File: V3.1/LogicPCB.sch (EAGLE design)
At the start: 65 parts, among them CON1 CUBE_ORANGE_, CON10 PINHEAD_1X02-2.54, CON11 CON-4P-JST-XA, CON12 PINHEAD_1X06-2.54, CON13 CON-6P-JST-XA, CON14 PINHEAD_1X04-2.54, CON15 CON-4P-JST-XA, CON17 CON-4P-JST-XA, CON18 CON-6P-JST-XA, CON19 USB-TYPE-C-VERT-PROD, CON2 CON-4P-JST-XA, CON20 PINHEAD_1X06-2.54, CON21 CON-4P-JST-XA, CON22 CON-4P-JST-XA, CON23 CON-4P-JST-XA, CON24 CON-4P-JST-XA, CON25 CON-4P-JST-XA, CON26 CON-4P-JST-XA, CON27 CON-4P-JST-XA, CON28 CON-4P-JST-XA, CON29 CON-4P-JST-XA, CON3 RJ45-NO_SHIELD-5556416-1, CON30 CON-4P-JST-XA, CON32 CON-4P-JST-XA, CON35 CON-12P-JST-XA, CON4 CON-2P-JST-XA, CON5 CON-6P-JST-XA, CON6 CON-4P-JST-XA, CON7 PINHEAD_1X06-2.54, CON9 PINHEAD_1X12-2.54, IC5 AOZ1280, M1 05G_ETHERNET_SWITCH, Q1 IRLML0030, T1 H1102NL, T2 H1102NL, T3 H1102NL, T4 H1102NL

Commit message: uarts
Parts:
- added R4, R5: (no value), rc:R-1%-0603
- added R6, R7: 000, rc:R-1%-0603
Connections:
- new net N$10: CON18.4, R5.1
- new net N$9: CON18.3, R4.1
- net GND: no longer CON35.10
- net HLK_RX0: now also CON35.6
- net HLK_RX1: now also R6.1
- net HLK_TX0: now also CON35.5
- net HLK_TX1: now also R7.1
- net SERIAL1_RX: now also R5.2, R7.2; no longer CON18.4
- net SERIAL1_TX: now also R4.2, R6.2; no longer CON18.3
- net SERIAL3_RX: now also CON35.8; no longer CON35.6
- net SERIAL3_TX: now also CON35.7; no longer CON35.5
- net VDD_24V: now also CON35.10; no longer CON35.7, CON35.8

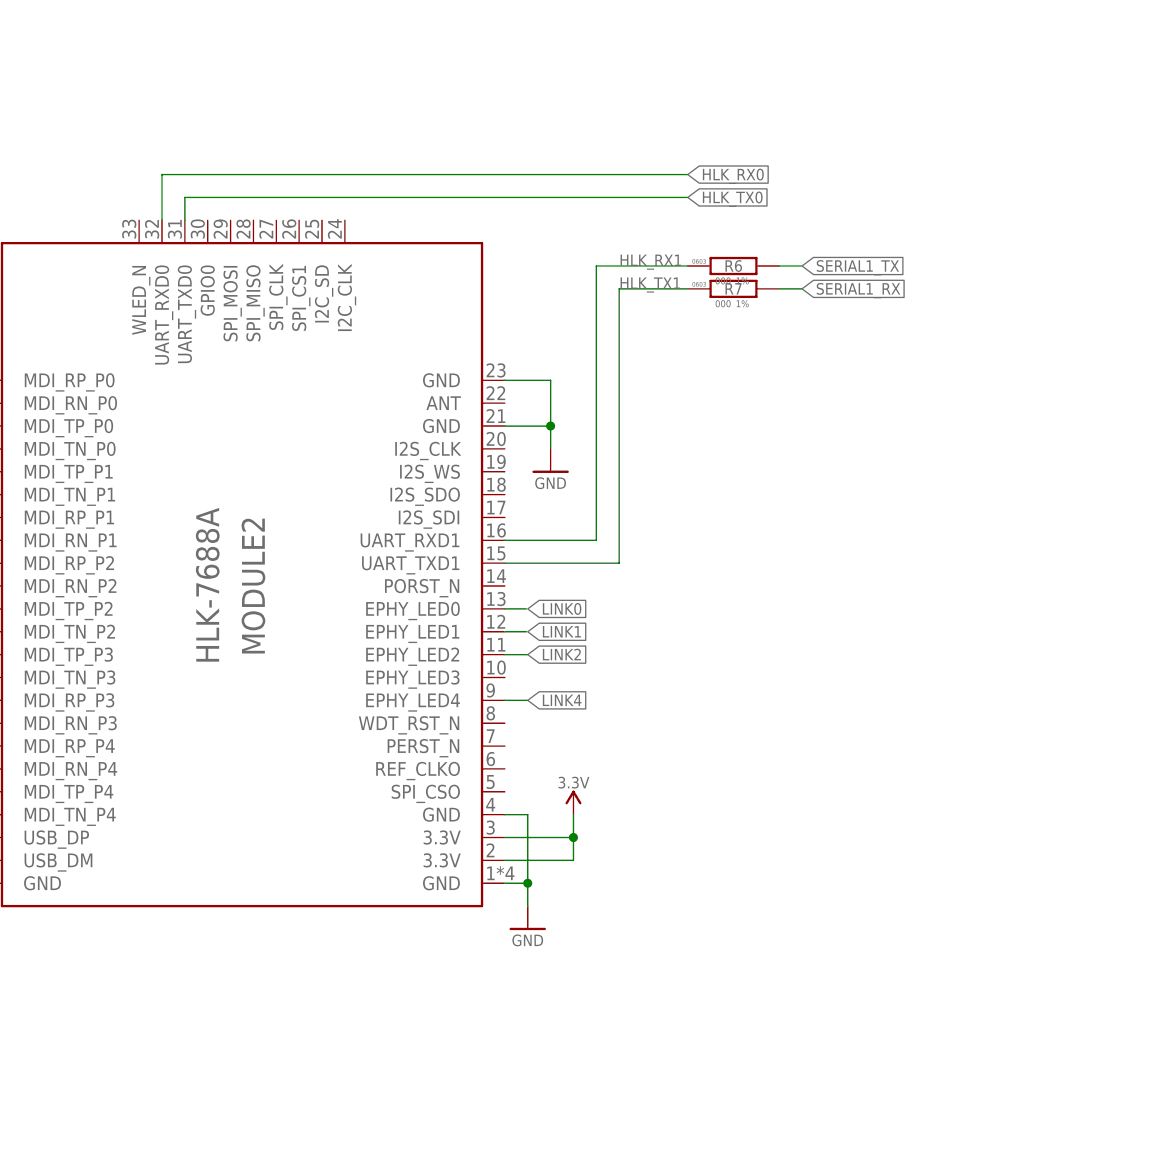
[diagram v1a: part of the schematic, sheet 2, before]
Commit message: link leds added
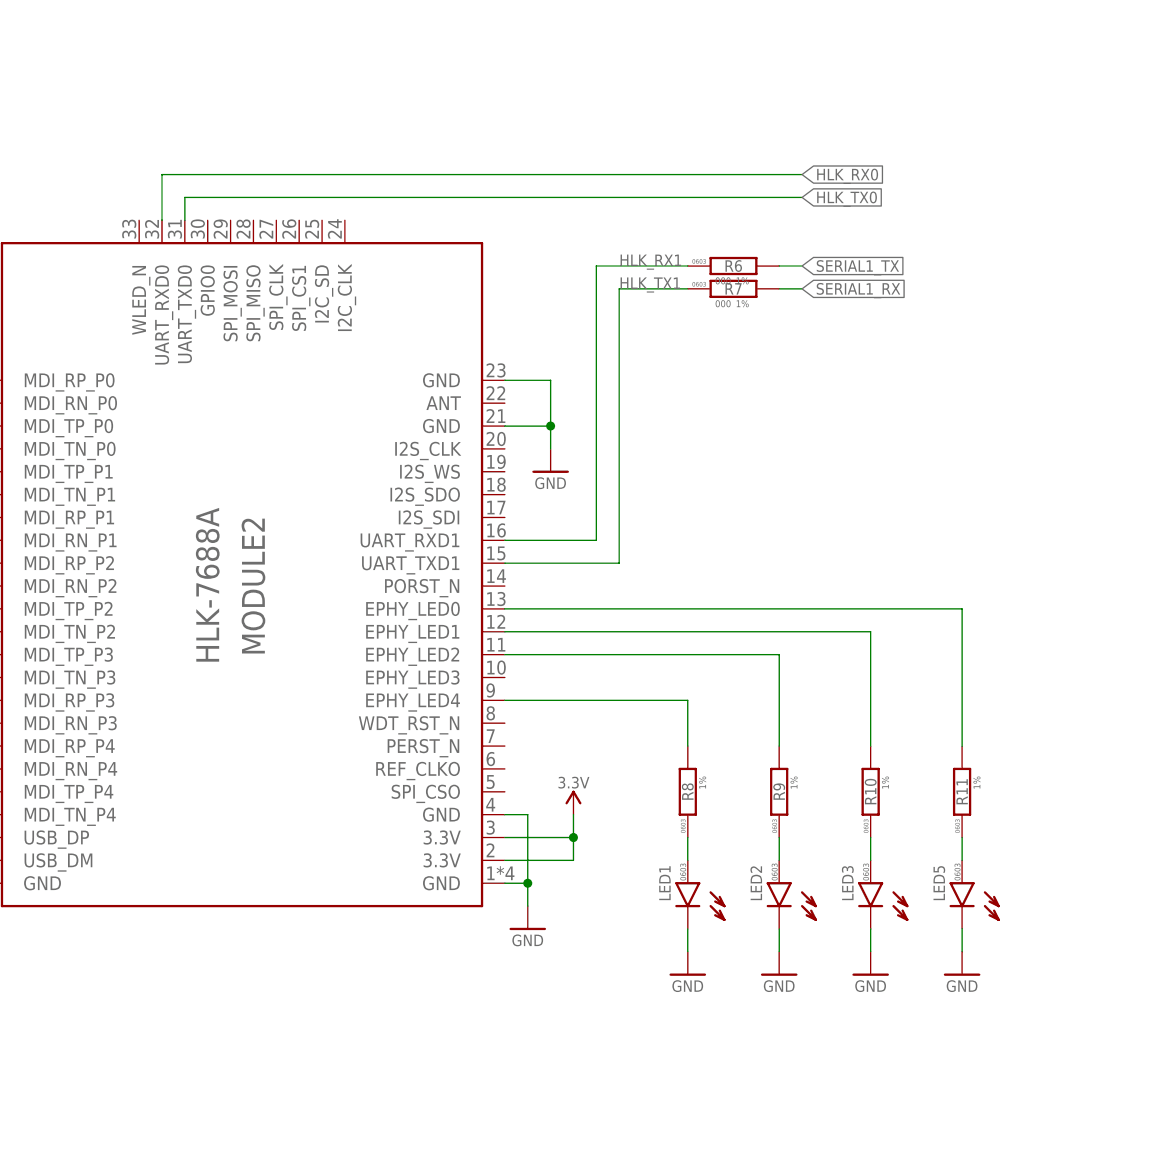
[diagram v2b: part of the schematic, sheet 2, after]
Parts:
- added LED1, LED2, LED3, LED5: LED-0603, rc:LED-0603
- added R10, R11, R8, R9: (no value), rc:R-1%-0603
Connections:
- removed net LINK0: MODULE2.EPHY_LED0
- removed net LINK1: MODULE2.EPHY_LED1
- new net N$11: LED1.A, R8.1
- new net N$12: LED2.A, R9.1
- new net N$14: LED3.A, R10.1
- new net N$15: LED5.A, R11.1
- new net N$16: MODULE2.EPHY_LED1, R10.2
- new net N$17: MODULE2.EPHY_LED0, R11.2
- net GND: now also LED1.C, LED2.C, LED3.C, LED5.C
- net LINK2: now also R9.2
- net LINK4: now also R8.2

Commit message: attribute updates
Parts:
- added D2, D3: ESDA5V3L, TVS_diodes:ESDA5V3L
- added PAD1, PAD2: PAD-HEX-2MM, PADS:PAD-HEX-2MM
- added R12, R14, R15: 120R, rc:R-1%-0603
- D1: value MBR0520L-SOD123 -> SS34; device Diodes:MBR0520L-SOD123 -> Diodes:SS34
- LED1, LED2, LED3, LED5: COLOR (none) -> RED; LCSC# (none) -> C2286; MANF (none) -> Hubei KENTO Elec; MANF# (none) -> KT-0603R
- R1, R3, R6, R7: value 000 -> 120R; ALLOCATED (none) -> +; LCSC# (none) -> C22787; MANF (none) -> UNI-ROYAL(Uniroyal Elec); MANF# (none) -> 0603WAF1200T5E
- R10, R11, R8, R9: value (none) -> 1K; ALLOCATED (none) -> +; LCSC# (none) -> C21190; MANF (none) -> UNI-ROYAL(Uniroyal Elec); MANF# (none) -> 0603WAF1001T5E
- R16: value 10K -> 51K; LCSC# (none) -> C23196
- R20: value 200R -> 120R; LCSC# C21190 -> C22787; MANF# 0603WAF1001T5E -> 0603WAF1200T5E
- R30, R31, R32: ALLOCATED (none) -> +
- R35, R36, R37, R38: value 100R -> 120R; ALLOCATED (none) -> +; LCSC# (none) -> C22787; MANF (none) -> UNI-ROYAL(Uniroyal Elec); MANF# (none) -> 0603WAF1200T5E
- R4, R5: value (none) -> 120R; ALLOCATED (none) -> +; LCSC# (none) -> C22787; MANF (none) -> UNI-ROYAL(Uniroyal Elec); MANF# (none) -> 0603WAF1200T5E
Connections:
- new net N$18: CON18.5, R12.1
- net GND: now also D2.A, D3.A
- net HLK_RX0: now also R14.1
- net HLK_TX0: now also R15.1
- net PPM-SBUS-PROT: now also D3.C, R12.2; no longer CON18.5
- net RX_2: now also R14.2
- net SERIAL1_RX: now also D2.C
- net SERIAL1_TX: now also D2.C1
- net TX_2: now also R15.2
- net USB_DM: now also PAD2.P$1
- net USB_DP: now also PAD1.P$1
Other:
- moved on the sheet: CON2, LED1, LED2, LED3, LED5, M1G$1, MODULE2, R10, R11, R3, R4, R5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

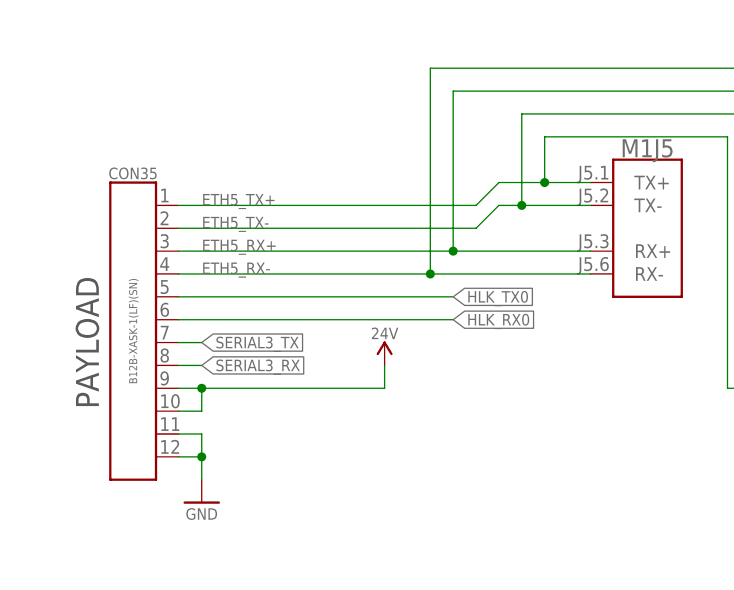
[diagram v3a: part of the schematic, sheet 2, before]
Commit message: Payload connector replaced with 2 6-pin ones
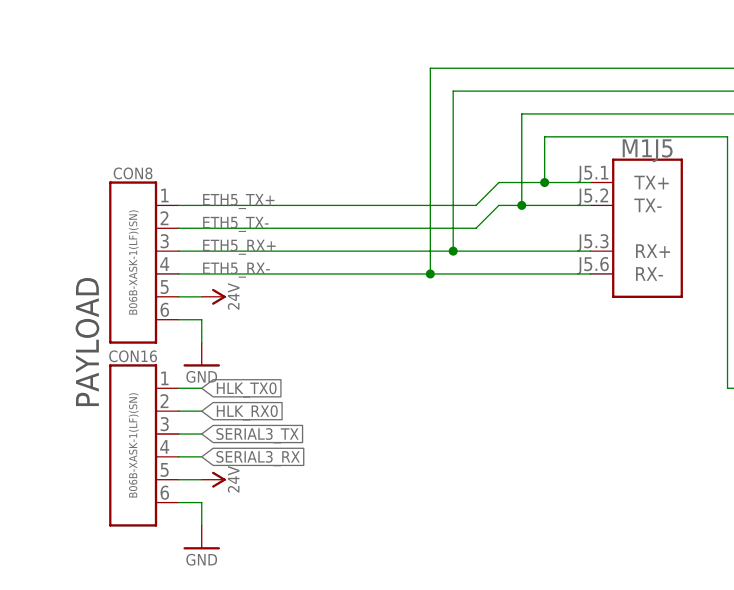
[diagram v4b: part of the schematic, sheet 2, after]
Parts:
- removed CON35: CON-12P-JST-XA, Connectors:CON-12P-JST-XA
- added CON16, CON8: CON-6P-JST-XA, Connectors:CON-6P-JST-XA
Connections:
- net ETH5_RX+: now also CON8.3; no longer CON35.3
- net ETH5_RX-: now also CON8.4; no longer CON35.4
- net ETH5_TX+: now also CON8.1; no longer CON35.1
- net ETH5_TX-: now also CON8.2; no longer CON35.2
- net GND: now also CON16.6, CON8.6; no longer CON35.11, CON35.12
- net HLK_RX0: now also CON16.2; no longer CON35.6
- net HLK_TX0: now also CON16.1; no longer CON35.5
- net SERIAL3_RX: now also CON16.4; no longer CON35.8
- net SERIAL3_TX: now also CON16.3; no longer CON35.7
- net VDD_24V: now also CON16.5, CON8.5; no longer CON35.10, CON35.9
